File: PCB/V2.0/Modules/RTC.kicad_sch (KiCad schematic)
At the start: 7 parts, among them U14 DS1307+, Y2 16MHz

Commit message: Add RTC
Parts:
- removed C2: 100nF, Capacitor_SMD:C_0603_1608Metric, symbol Device:C
- BT1: footprint Battery:Battery_Panasonic_CR2032-HFN_Horizontal_CircularHoles -> BC501SM:MPD_BC501SM-TR
- R27: footprint Resistor_THT:R_Axial_DIN0207_L6.3mm_D2.5mm_P7.62mm_Horizontal -> Resistor_THT:R_Axial_DIN0207_L6.3mm_D2.5mm_P10.16mm_Horizontal
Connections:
- net +3.3V: no longer U14.8 (VCC)
- net GND: now also BT1.2 (-)
- net at U14.3 (VBAT): now also BT1.1 (+)
- new net +5V: U14.8 (VCC)
- no-connect marks 1 -> 0
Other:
- moved on the sheet: BT1
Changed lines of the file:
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@@
 		(company "Designed by CREPP-NLG")
-	)
-	(junction
-		(at 90.17 52.07)
-		(diameter 0)
-		(color 0 0 0 0)
-	)
-	(no_connect
-		(at 96.52 55.88)
 	)
 	(bus_entry
@@
 	(wire
 		(pts
+			(xy 96.52 55.88) (xy 96.52 48.26)
+		)
+		(stroke
+			(width 0)
+			(type default)
+		)
+	)
+	(wire
+		(pts
 			(xy 96.52 76.2) (xy 96.52 80.01)
 		)
@@
 	(wire
 		(pts
-			(xy 90.17 50.8) (xy 90.17 52.07)
-		)
-		(stroke
-			(width 0)
-			(type default)
-		)
-	)
-	(wire
-		(pts
 			(xy 72.39 76.2) (xy 72.39 68.58)
 		)
@@
 	(wire
 		(pts
-			(xy 90.17 36.83) (xy 90.17 43.18)
+			(xy 107.95 48.26) (xy 110.49 48.26)
 		)
 		(stroke
@@
 	(wire
 		(pts
+			(xy 96.52 48.26) (xy 100.33 48.26)
+		)
+		(stroke
+			(width 0)
+			(type default)
+		)
+	)
+	(wire
+		(pts
 			(xy 93.98 52.07) (xy 93.98 55.88)
 		)
@@
 	(wire
 		(pts
-			(xy 82.55 52.07) (xy 90.17 52.07)
-		)
-		(stroke
-			(width 0)
-			(type default)
-		)
-	)
-	(wire
-		(pts
-			(xy 90.17 52.07) (xy 93.98 52.07)
+			(xy 82.55 52.07) (xy 93.98 52.07)
 		)
 		(stroke
@@
 		)
 	)
+	(label "GND"
+		(at 110.49 48.26 0)
+		(fields_autoplaced yes)
+		(effects
+			(font
+				(size 1.27 1.27)
+			)
+			(justify left bottom)
+		)
+	)
 	(label "SDA"
 		(at 63.5 63.5 0)
@@
 	(label "GND"
 		(at 52.07 80.01 0)
-		(fields_autoplaced yes)
-		(effects
-			(font
-				(size 1.27 1.27)
-			)
-			(justify left bottom)
-		)
-	)
-	(label "GND"
-		(at 90.17 36.83 0)
 		(fields_autoplaced yes)
 		(effects
@@
 		)
 	)
-	(hierarchical_label "+3.3V"
+	(hierarchical_label "+5V"
 		(shape input)
 		(at 82.55 52.07 180)
@@
 	(symbol
 		(lib_id "Device:Battery_Cell")
-		(at 137.16 90.17 0)
+		(at 105.41 48.26 90)
 		(unit 1)
 		(exclude_from_sim no)
@@
 		(fields_autoplaced yes)
 		(property "Reference" "BT1"
-			(at 140.97 87.0584 0)
-			(effects
-				(font
-					(size 1.27 1.27)
-				)
-				(justify left)
+			(at 103.5685 40.64 90)
+			(effects
+				(font
+					(size 1.27 1.27)
+				)
 			)
 		)
 		(property "Value" "Battery_Cell"
-			(at 140.97 89.5984 0)
-			(effects
-				(font
-					(size 1.27 1.27)
-				)
-				(justify left)
-			)
-		)
-		(property "Footprint" "Battery:Battery_Panasonic_CR2032-HFN_Horizontal_CircularHoles"
-			(at 137.16 88.646 90)
+			(at 103.5685 43.18 90)
+			(effects
+				(font
+					(size 1.27 1.27)
+				)
+			)
+		)
+		(property "Footprint" "BC501SM:MPD_BC501SM-TR"
+			(at 103.886 48.26 90)
 			(effects
 				(font
@@
 		)
 		(property "Datasheet" "~"
-			(at 137.16 88.646 90)
+			(at 103.886 48.26 90)
 			(effects
 				(font
@@
 		)
 		(property "Description" "Single-cell battery"
-			(at 137.16 90.17 0)
+			(at 105.41 48.26 0)
 			(effects
 				(font
@@
 	)
 	(symbol
-		(lib_id "Device:C")
-		(at 90.17 46.99 180)
-		(unit 1)
-		(exclude_from_sim no)
-		(in_bom yes)
-		(on_board yes)
-		(dnp no)
-		(fields_autoplaced yes)
-		(property "Reference" "C2"
-			(at 93.98 45.7199 0)
-			(effects
-				(font
-					(size 1.27 1.27)
-				)
-				(justify right)
-			)
-		)
-		(property "Value" "100nF"
-			(at 93.98 48.2599 0)
-			(effects
-				(font
-					(size 1.27 1.27)
-				)
-				(justify right)
-			)
-		)
-		(property "Footprint" "Capacitor_SMD:C_0603_1608Metric"
-			(at 89.2048 43.18 0)
-			(effects
-				(font
-					(size 1.27 1.27)
-				)
-				(hide yes)
-			)
-		)
-		(property "Datasheet" "~"
-			(at 90.17 46.99 0)
-			(effects
-				(font
-					(size 1.27 1.27)
-				)
-				(hide yes)
-			)
-		)
-		(property "Description" "Unpolarized capacitor"
-			(at 90.17 46.99 0)
-			(effects
-				(font
-					(size 1.27 1.27)
-				)
-				(hide yes)
-			)
-		)
-		(pin "2"
-		)
-		(pin "1"
-		)
-		(instances
-			(project "CREPP.io"
-				(path "/8bcd0d00-b75f-4070-8d50-196a2022a31c/7d5e0927-d56c-4e49-a3db-e12f7a1550df"
-					(reference "C2")
-					(unit 1)
-				)
-			)
-		)
-	)
-	(symbol
 		(lib_id "Device:R")
 		(at 129.54 62.23 0)
@@
 			)
 		)
-		(property "Footprint" "Resistor_THT:R_Axial_DIN0207_L6.3mm_D2.5mm_P7.62mm_Horizontal"
+		(property "Footprint" "Resistor_THT:R_Axial_DIN0207_L6.3mm_D2.5mm_P10.16mm_Horizontal"
 			(at 127.762 62.23 90)
 			(effects

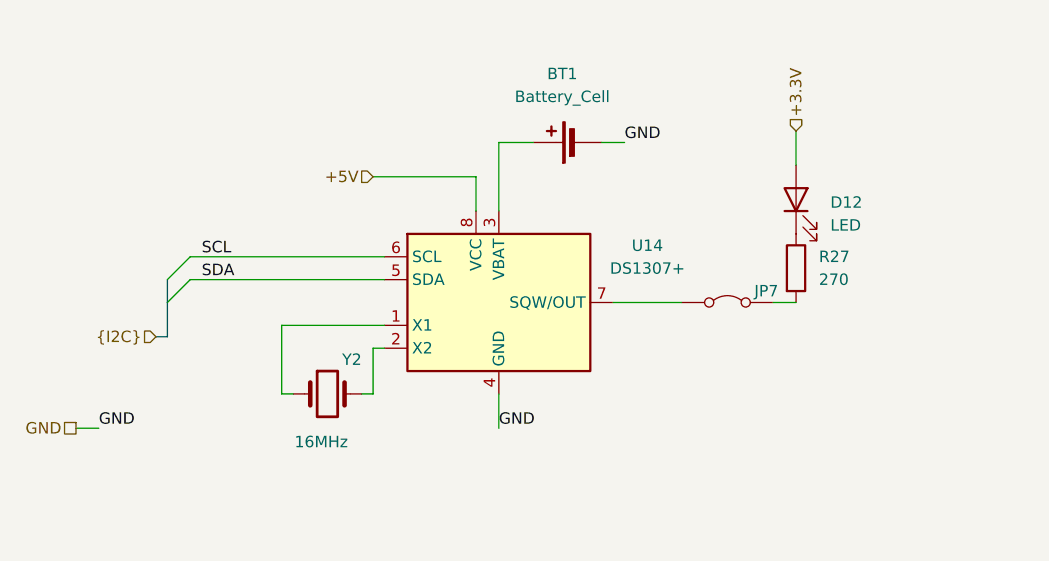
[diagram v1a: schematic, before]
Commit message: Update V2.0 form factor
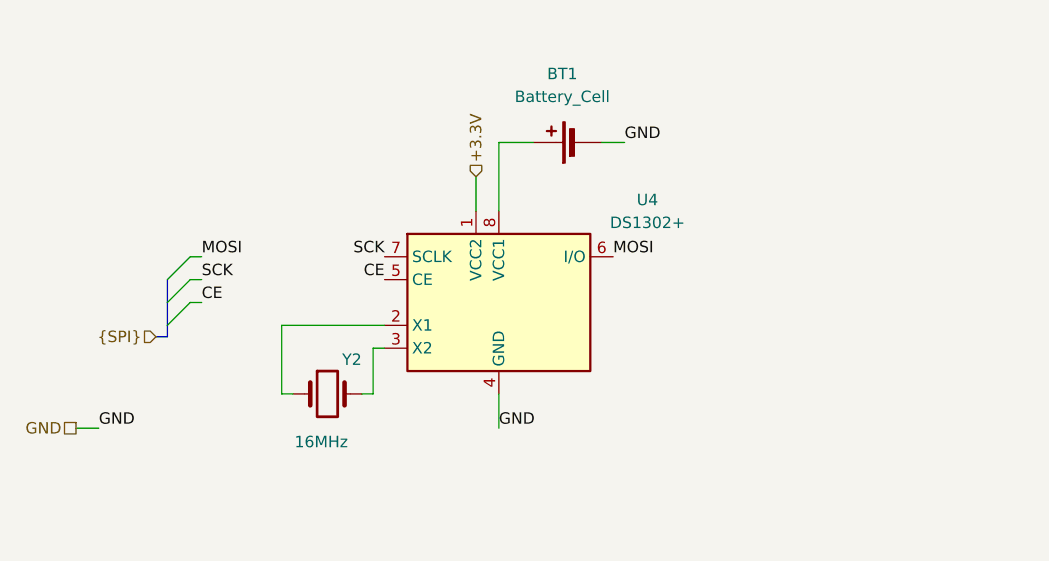
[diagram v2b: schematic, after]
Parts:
- removed D12: LED, LED_THT:LED_D5.0mm, symbol Device:LED
- removed JP7: Jumper, Connector_PinHeader_2.54mm:PinHeader_1x02_P2.54mm_Vertical, symbol Jumper:Jumper_2_Bridged
- removed R27: 270, Resistor_THT:R_Axial_DIN0207_L6.3mm_D2.5mm_P10.16mm_Horizontal, symbol Device:R
- removed U14: DS1307+, Package_DIP:DIP-8_W7.62mm, symbol Timer_RTC:DS1307+
- added U4: DS1302+, Package_DIP:DIP-8_W7.62mm, symbol Timer_RTC:DS1302+
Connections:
- net +3.3V: now also U4.1 (VCC2)
- net GND: now also U4.4 (GND)
- net at Y2.1: now also U4.2 (X1)
- net at Y2.2: now also U4.3 (X2)
- net at BT1.1 (+): now also U4.8 (VCC1)
- new net CE: U4.5 (CE)
- new net MOSI: U4.6 (I/O)
- new net SCK: U4.7 (SCLK)

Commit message: Update board
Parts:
- removed BT1: Battery_Cell, BC501SM:MPD_BC501SM-TR, symbol Device:Battery_Cell
- removed U4: DS1302+, Package_DIP:DIP-8_W7.62mm, symbol Timer_RTC:DS1302+
- removed Y2: 16MHz, Crystal:Crystal_AT310_D3.0mm_L10.0mm_Horizontal, symbol Device:Crystal
- added BT1: Battery_Cell, CREPP_Batteries_holders:MPD_BC501SM-TR, symbol CREPP_Batteries_holders:Battery_Cell
- added D8: LED, LED_THT:LED_D5.0mm, symbol Device:LED
- added R9: 270, Resistor_THT:R_Axial_DIN0207_L6.3mm_D2.5mm_P10.16mm_Horizontal, symbol Device:R
- added U4: DS3231M, Package_SO:SOIC-16W_7.5x10.3mm_P1.27mm, symbol CREPP_RTC:DS3231M
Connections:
- net +3.3V: now also U4.2 (VCC), U4.4 (~{RST})
- net GND: now also BT1.2 (-), R9.2, U4.10 (GND), U4.11 (GND), U4.12 (GND), U4.13 (GND), U4.5 (GND), U4.6 (GND), U4.7 (GND), U4.8 (GND), U4.9 (GND)
- new net: BT1.1 (+), U4.14 (VBAT)
- new net: D8.1 (K), R9.1
- new net: D8.2 (A), U4.3 (~{INT}/SQW)
- new net SCL: U4.16 (SCL)
- new net SDA: U4.15 (SDA)
- no-connect marks 0 -> 1

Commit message: Update
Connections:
- net +3.3V: now also R9.2
- net GND: no longer R9.2
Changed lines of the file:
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@@
 	(wire
 		(pts
-			(xy 127 68.58) (xy 129.54 68.58)
+			(xy 127 68.58) (xy 140.97 68.58)
 		)
 		(stroke
@@
 	)
 	(label "GND"
-		(at 129.54 68.58 0)
-		(effects
-			(font
-				(size 1.27 1.27)
-			)
-			(justify left bottom)
-		)
-	)
-	(label "GND"
 		(at 96.52 80.01 0)
 		(effects
@@
 		)
 	)
+	(label "+3.3V"
+		(at 140.97 68.58 180)
+		(effects
+			(font
+				(size 1.27 1.27)
+			)
+			(justify right bottom)
+		)
+	)
